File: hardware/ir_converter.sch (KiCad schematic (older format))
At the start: 47 parts, among them J1 MX-47346-0001, J2 SWD, J3 TP, J4 TP, Q1 LL-S350PTC-1A, SW1 RESET, SW2 SW2, U1 TLV70033DDCT, U2 USBLC6-2, U3 STM32F103C8T6

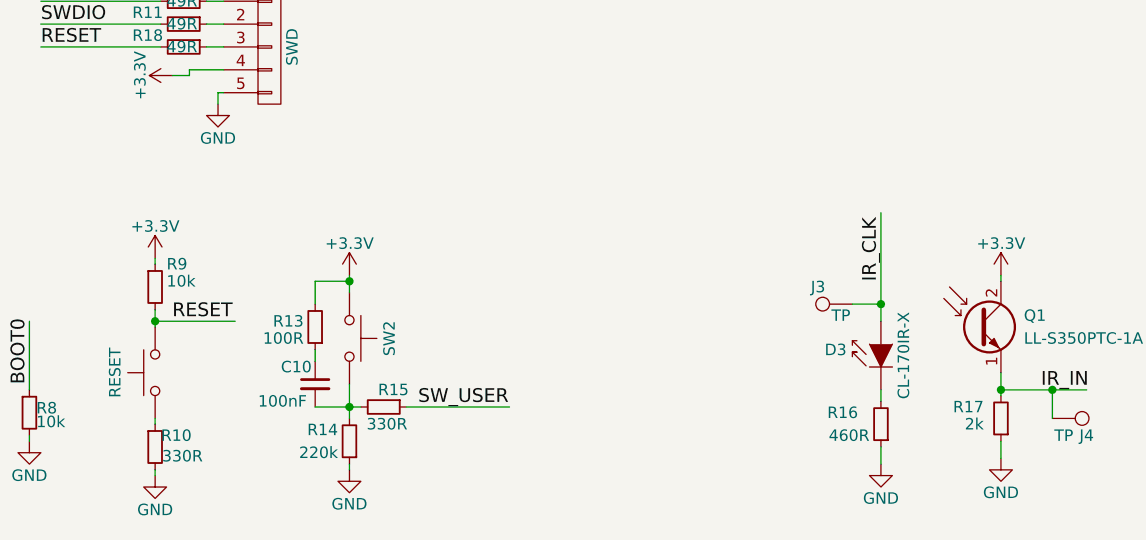
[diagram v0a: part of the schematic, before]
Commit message: Added npn tranistor to drive the IR LED.
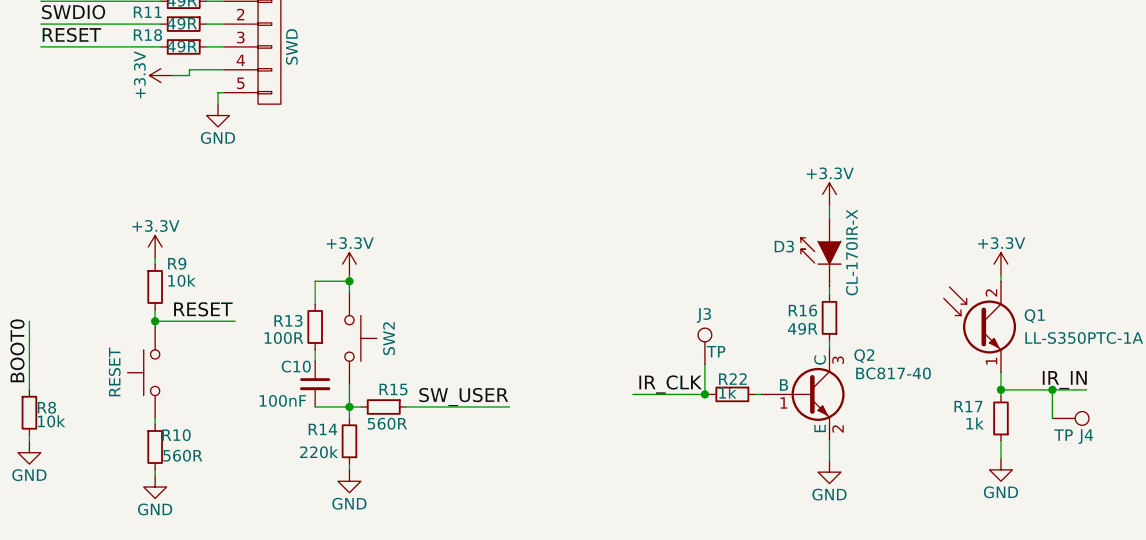
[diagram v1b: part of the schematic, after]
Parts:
- added Q2: BC817-40, TO_SOT_Packages_SMD:SOT-23, symbol BC817-40
- added R22: 1k, Resistors_SMD:R_0603_HandSoldering, symbol R_Small
- R10, R15: value 330R -> 560R
- R16: value 460R -> 49R
- R17: value 2k -> 1k
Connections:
- wire segments 133 -> 136
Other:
- moved on the sheet: D3, J3, R16
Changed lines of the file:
@@
 L IR204A D3
 U 1 1 58E6638F
-P 5725 7000
-F 0 "D3" V 5700 7150 50  0000 L CNN
-F 1 "CL-170IR-X" H 5675 6900 50  0000 C CNN
-F 2 "LEDs:LED_0805" H 5725 7175 50  0001 C CNN
-F 3 "" H 5675 7000 50  0000 C CNN
-	1    5725 7000
+P 5500 6550
+F 0 "D3" V 5475 6700 50  0000 L CNN
+F 1 "CL-170IR-X" H 5450 6450 50  0000 C CNN
+F 2 "LEDs:LED_0805" H 5500 6725 50  0001 C CNN
+F 3 "" H 5450 6550 50  0000 C CNN
+	1    5500 6550
 	0    -1   -1   0
 $EndComp
@@
 L R_Small R16
 U 1 1 58E67683
-P 5725 7350
-F 0 "R16" H 5825 7300 50  0000 L CNN
-F 1 "460R" H 5775 7400 50  0000 L CNN
-F 2 "Resistors_SMD:R_0603_HandSoldering" H 5725 7350 50  0001 C CNN
-F 3 "" H 5725 7350 50  0001 C CNN
-	1    5725 7350
+P 5500 6885
+F 0 "R16" H 5550 6855 50  0000 L CNN
+F 1 "49R" H 5550 6935 50  0000 L CNN
+F 2 "Resistors_SMD:R_0603_HandSoldering" H 5500 6885 50  0001 C CNN
+F 3 "" H 5500 6885 50  0001 C CNN
+	1    5500 6885
 	-1   0    0    1
 $EndComp
@@
 L GND #PWR023
 U 1 1 58E6782D
-P 5725 7525
-F 0 "#PWR023" H 5725 7275 50  0001 C CNN
-F 1 "GND" H 5725 7375 50  0000 C CNN
-F 2 "" H 5725 7525 50  0001 C CNN
-F 3 "" H 5725 7525 50  0001 C CNN
-	1    5725 7525
+P 5500 7510
+F 0 "#PWR023" H 5500 7260 50  0001 C CNN
+F 1 "GND" H 5500 7360 50  0000 C CNN
+F 2 "" H 5500 7510 50  0001 C CNN
+F 3 "" H 5500 7510 50  0001 C CNN
+	1    5500 7510
 	1    0    0    -1
 $EndComp
@@
 P 6250 7325
 F 0 "R17" H 6325 7275 50  0000 L CNN
-F 1 "2k" H 6325 7350 50  0000 L CNN
+F 1 "1k" H 6325 7350 50  0000 L CNN
 F 2 "Resistors_SMD:R_0603_HandSoldering" H 6250 7325 50  0001 C CNN
 F 3 "" H 6250 7325 50  0001 C CNN
@@
 P 2550 7450
 F 0 "R10" H 2575 7500 50  0000 L CNN
-F 1 "330R" H 2580 7410 50  0000 L CNN
+F 1 "560R" H 2580 7410 50  0000 L CNN
 F 2 "Resistors_SMD:R_0603_HandSoldering" H 2550 7450 50  0001 C CNN
 F 3 "" H 2550 7450 50  0001 C CNN
@@
 P 3550 7275
 F 0 "R15" V 3475 7250 50  0000 L CNN
-F 1 "330R" V 3625 7200 50  0000 L CNN
+F 1 "560R" V 3625 7200 50  0000 L CNN
 F 2 "Resistors_SMD:R_0603_HandSoldering" H 3550 7275 50  0001 C CNN
 F 3 "" H 3550 7275 50  0001 C CNN
@@
 Text Label 4100 3300 0    60   ~ 0
 IR_CLK
-Text Label 5725 6725 1    60   ~ 0
+Text Label 4940 7220 2    60   ~ 0
 IR_CLK
 Text Label 6425 7200 0    60   ~ 0
@@
 L TEST_1P J3
 U 1 1 58E9EED0
-P 5600 6825
-F 0 "J3" V 5675 6975 50  0000 C CNN
-F 1 "TP" V 5550 6875 50  0000 C CNN
-F 2 "Measurement_Points:Measurement_Point_Square-SMD-Pad_Big" H 5800 6825 50  0001 C CNN
-F 3 "" H 5800 6825 50  0001 C CNN
-	1    5600 6825
-	0    -1   -1   0
+P 4955 7090
+F 0 "J3" H 4955 7310 50  0000 C CNN
+F 1 "TP" H 5005 7145 50  0000 C CNN
+F 2 "Measurement_Points:Measurement_Point_Square-SMD-Pad_Big" H 5155 7090 50  0001 C CNN
+F 3 "" H 5155 7090 50  0001 C CNN
+	1    4955 7090
+	1    0    0    -1
 $EndComp
 $Comp
@@
 	10400 4300 10875 4300
 Wire Wire Line
-	5725 7450 5725 7525
-Wire Wire Line
-	5725 7250 5725 7200
-Wire Wire Line
-	5725 6425 5725 6900
+	5500 6985 5500 7020
+Wire Wire Line
+	5500 6785 5500 6750
+Wire Wire Line
+	5500 6395 5500 6450
 Wire Wire Line
 	4100 3300 4600 3300
@@
 Wire Wire Line
 	2750 3300 3125 3300
-Wire Wire Line
-	5600 6825 5725 6825
-Connection ~ 5725 6825
 Wire Wire Line
 	6475 7325 6475 7200
@@
 	0    1    1    0
 $EndComp
+$Comp
+L BC817-40 Q2
+U 1 1 590A0634
+P 5400 7220
+F 0 "Q2" H 5605 7390 50  0000 L CNN
+F 1 "BC817-40" H 5610 7310 50  0000 L CNN
+F 2 "TO_SOT_Packages_SMD:SOT-23" H 5600 7145 50  0001 L CIN
+F 3 "" H 5400 7220 50  0001 L CNN
+	1    5400 7220
+	1    0    0    -1
+$EndComp
+Wire Wire Line
+	5500 7420 5500 7510
+$Comp
+L R_Small R22
+U 1 1 590A3C87
+P 5075 7220
+F 0 "R22" V 5010 7155 50  0000 L CNN
+F 1 "1k" V 5070 7155 50  0000 L CNN
+F 2 "Resistors_SMD:R_0603_HandSoldering" H 5075 7220 50  0001 C CNN
+F 3 "" H 5075 7220 50  0001 C CNN
+	1    5075 7220
+	0    1    1    0
+$EndComp
+Wire Wire Line
+	5175 7220 5200 7220
+Wire Wire Line
+	4640 7220 4975 7220
+$Comp
+L +3.3V #PWR035
+U 1 1 590A61E3
+P 5500 6395
+F 0 "#PWR035" H 5500 6245 50  0001 C CNN
+F 1 "+3.3V" H 5500 6535 50  0000 C CNN
+F 2 "" H 5500 6395 50  0001 C CNN
+F 3 "" H 5500 6395 50  0001 C CNN
+	1    5500 6395
+	1    0    0    -1
+$EndComp
+Wire Wire Line
+	4955 7090 4955 7220
+Connection ~ 4955 7220
 $EndSCHEMATC

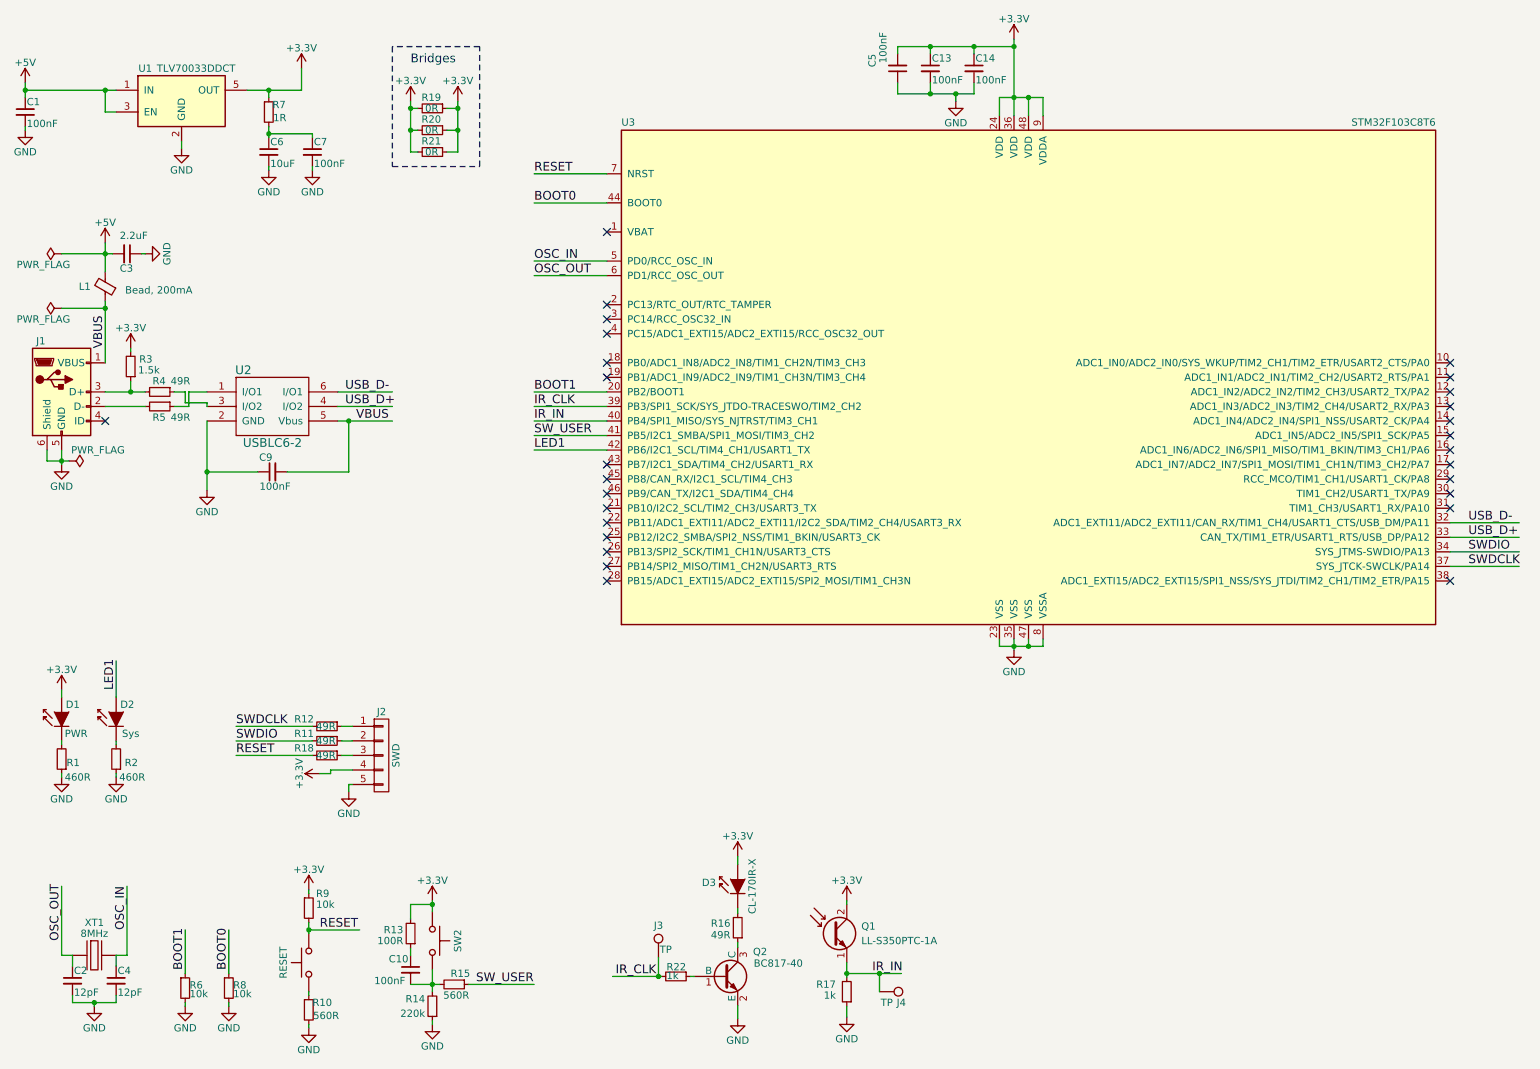
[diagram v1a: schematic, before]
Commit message: Added bug fixes on schematic. Redesigning PCB.
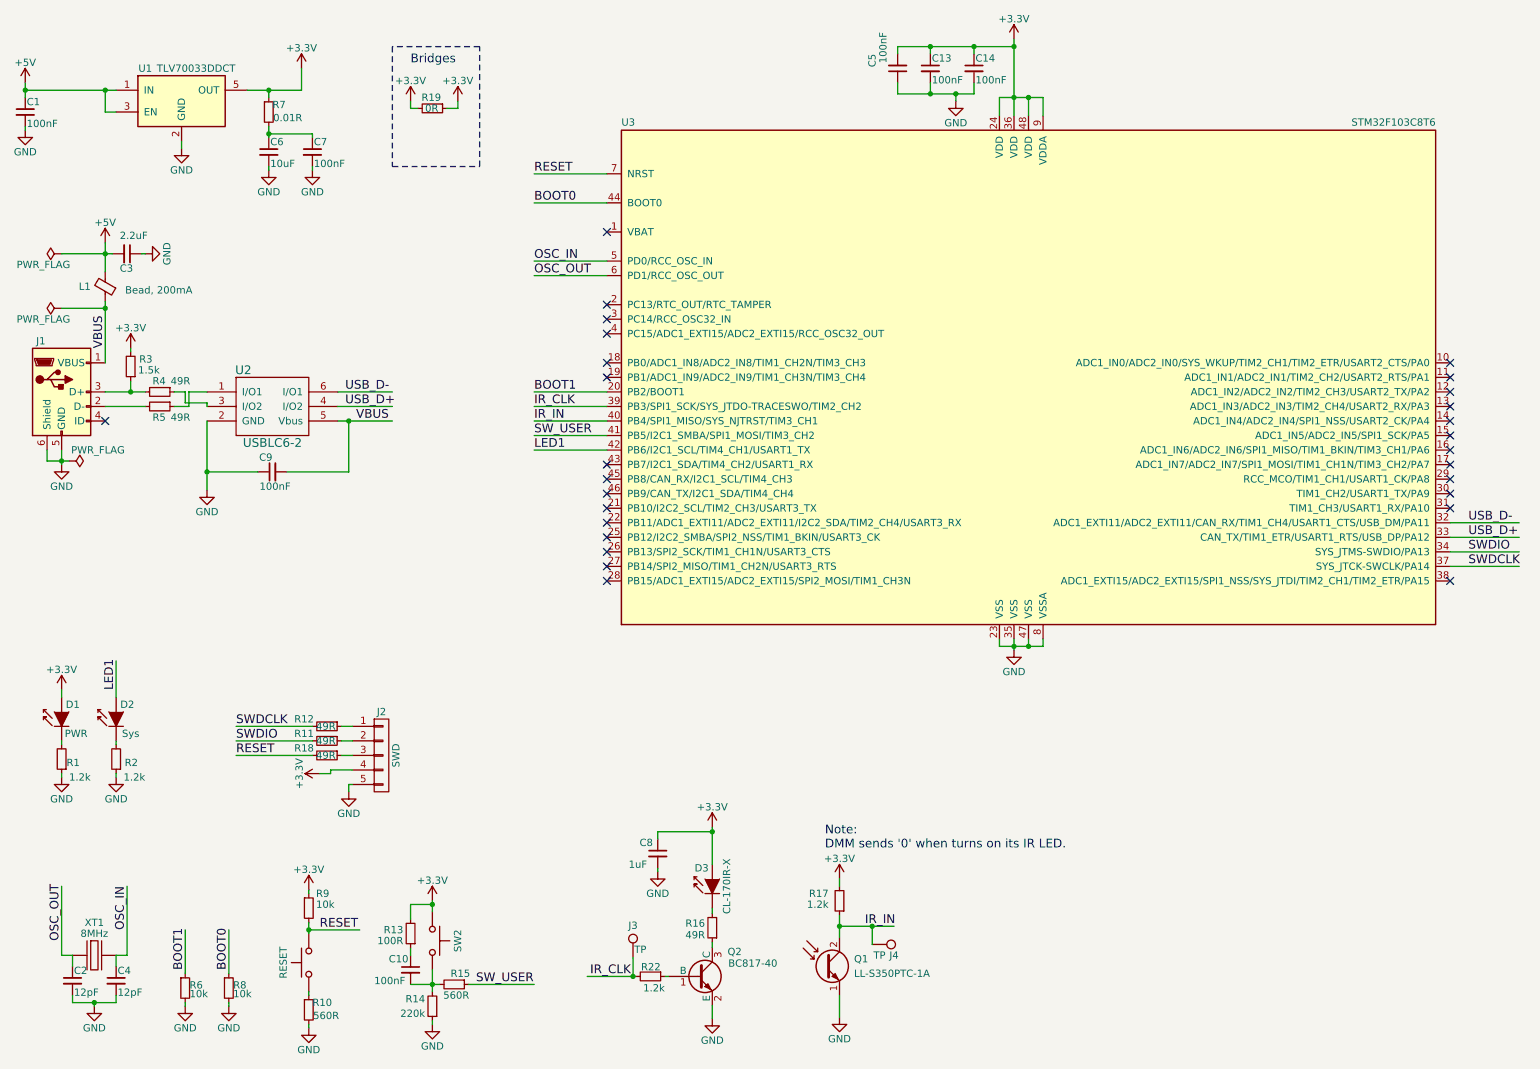
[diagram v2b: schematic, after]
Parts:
- removed R20, R21: 0R, Resistors_SMD:R_1206_HandSoldering, symbol R_Small
- added C8: 1uF, Capacitors_SMD:C_0603_HandSoldering, symbol C_Small
- C14: footprint Capacitors_SMD:C_1206_HandSoldering -> Capacitors_SMD:C_0603_HandSoldering
- C6: footprint Capacitors_SMD:C_1206 -> Capacitors_SMD:C_0603_HandSoldering
- D1, D2: footprint LEDs:LED_0805 -> LEDs:LED_1206
- J3, J4: footprint Measurement_Points:Measurement_Point_Square-SMD-Pad_Big -> Measurement_Points:Measurement_Point_Square-SMD-Pad_Small
- R1, R2: value 460R -> 1.2k
- R17, R22: value 1k -> 1.2k
- R6: footprint Resistors_SMD:R_0805 -> Resistors_SMD:R_0603_HandSoldering
- R7: value 1R -> 0.01R
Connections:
- wire segments 136 -> 135
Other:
- note added: "Note:\nDMM sends '0' when turns on its IR LED."
- moved on the sheet: D3, J3, J4, Q1, Q2, R16, R17, R22

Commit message: Elements arrangement.
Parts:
- removed R19: 0R, Resistors_SMD:R_1206_HandSoldering, symbol R_Small
- removed R7: 0.01R, Resistors_SMD:R_0603_HandSoldering, symbol R_Small
- R18: footprint Resistors_SMD:R_0805 -> Resistors_SMD:R_0603_HandSoldering
- R3: footprint Resistors_SMD:R_1206_HandSoldering -> Resistors_SMD:R_0603_HandSoldering
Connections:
- net labels added: S_D+, S_D-
- wire segments 135 -> 129
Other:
- note removed: "Bridges"
- moved on the sheet: C6, C7
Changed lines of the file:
@@
 L GND #PWR02
 U 1 1 58E4A167
-P 2275 1675
-F 0 "#PWR02" H 2275 1425 50  0001 C CNN
-F 1 "GND" H 2275 1525 50  0000 C CNN
-F 2 "" H 2275 1675 50  0001 C CNN
-F 3 "" H 2275 1675 50  0001 C CNN
-	1    2275 1675
-	1    0    0    -1
-$EndComp
-$Comp
-L R_Small R7
-U 1 1 58E4A190
-P 2275 1275
-F 0 "R7" H 2300 1325 50  0000 L CNN
-F 1 "0.01R" H 2305 1235 50  0000 L CNN
-F 2 "Resistors_SMD:R_0603_HandSoldering" H 2275 1275 50  0001 C CNN
-F 3 "" H 2275 1275 50  0001 C CNN
-	1    2275 1275
+P 2200 1450
+F 0 "#PWR02" H 2200 1200 50  0001 C CNN
+F 1 "GND" H 2200 1300 50  0000 C CNN
+F 2 "" H 2200 1450 50  0001 C CNN
+F 3 "" H 2200 1450 50  0001 C CNN
+	1    2200 1450
 	1    0    0    -1
 $EndComp
@@
 L C_Small C6
 U 1 1 58E4A225
-P 2275 1550
-F 0 "C6" H 2285 1620 50  0000 L CNN
-F 1 "10uF" H 2285 1470 50  0000 L CNN
-F 2 "Capacitors_SMD:C_0603_HandSoldering" H 2275 1550 50  0001 C CNN
-F 3 "" H 2275 1550 50  0001 C CNN
-	1    2275 1550
+P 2200 1325
+F 0 "C6" H 2210 1395 50  0000 L CNN
+F 1 "10uF" H 2210 1245 50  0000 L CNN
+F 2 "Capacitors_SMD:C_0603_HandSoldering" H 2200 1325 50  0001 C CNN
+F 3 "" H 2200 1325 50  0001 C CNN
+	1    2200 1325
 	1    0    0    -1
 $EndComp
@@
 L C_Small C7
 U 1 1 58E4A432
-P 2575 1550
-F 0 "C7" H 2585 1620 50  0000 L CNN
-F 1 "100nF" H 2585 1470 50  0000 L CNN
-F 2 "Capacitors_SMD:C_0603_HandSoldering" H 2575 1550 50  0001 C CNN
-F 3 "" H 2575 1550 50  0001 C CNN
-	1    2575 1550
+P 2425 1325
+F 0 "C7" H 2435 1395 50  0000 L CNN
+F 1 "100nF" H 2435 1245 50  0000 L CNN
+F 2 "Capacitors_SMD:C_0603_HandSoldering" H 2425 1325 50  0001 C CNN
+F 3 "" H 2425 1325 50  0001 C CNN
+	1    2425 1325
 	1    0    0    -1
 $EndComp
@@
 L GND #PWR04
 U 1 1 58E4A63E
-P 2575 1675
-F 0 "#PWR04" H 2575 1425 50  0001 C CNN
-F 1 "GND" H 2575 1525 50  0000 C CNN
-F 2 "" H 2575 1675 50  0001 C CNN
-F 3 "" H 2575 1675 50  0001 C CNN
-	1    2575 1675
+P 2425 1450
+F 0 "#PWR04" H 2425 1200 50  0001 C CNN
+F 1 "GND" H 2425 1300 50  0000 C CNN
+F 2 "" H 2425 1450 50  0001 C CNN
+F 3 "" H 2425 1450 50  0001 C CNN
+	1    2425 1450
 	1    0    0    -1
 $EndComp
@@
 F 0 "R3" H 1175 2975 50  0000 L CNN
 F 1 "1.5k" H 1125 3050 50  0000 L CNN
-F 2 "Resistors_SMD:R_1206_HandSoldering" H 1325 3025 50  0001 C CNN
+F 2 "Resistors_SMD:R_0603_HandSoldering" H 1325 3025 50  0001 C CNN
 F 3 "" H 1325 3025 50  0001 C CNN
 	1    1325 3025
@@
 F 0 "R18" V 2625 5475 50  0000 L CNN
 F 1 "49R" V 2675 5625 50  0000 L CNN
-F 2 "Resistors_SMD:R_0805" H 2675 5700 50  0001 C CNN
+F 2 "Resistors_SMD:R_0603_HandSoldering" H 2675 5700 50  0001 C CNN
 F 3 "" H 2675 5700 50  0001 C CNN
 	1    2675 5700
@@
 NoConn ~ 4600 4200
 $Comp
-L R_Small R19
-U 1 1 58E7CB35
-P 3400 1250
-F 0 "R19" V 3325 1175 50  0000 L CNN
-F 1 "0R" V 3400 1200 50  0000 L CNN
-F 2 "Resistors_SMD:R_1206_HandSoldering" H 3400 1250 50  0001 C CNN
-F 3 "" H 3400 1250 50  0001 C CNN
-	1    3400 1250
-	0    1    1    0
-$EndComp
-$Comp
-L +3.3V #PWR032
-U 1 1 58E7CECF
-P 3250 1200
-F 0 "#PWR032" H 3250 1050 50  0001 C CNN
-F 1 "+3.3V" H 3250 1340 50  0000 C CNN
-F 2 "" H 3250 1200 50  0001 C CNN
-F 3 "" H 3250 1200 50  0001 C CNN
-	1    3250 1200
-	1    0    0    -1
-$EndComp
-$Comp
-L +3.3V #PWR033
-U 1 1 58E7CF5E
-P 3575 1200
-F 0 "#PWR033" H 3575 1050 50  0001 C CNN
-F 1 "+3.3V" H 3575 1340 50  0000 C CNN
-F 2 "" H 3575 1200 50  0001 C CNN
-F 3 "" H 3575 1200 50  0001 C CNN
-	1    3575 1200
-	1    0    0    -1
-$EndComp
-$Comp
-L PWR_FLAG #FLG034
+L PWR_FLAG #FLG032
 U 1 1 58E7DF60
 P 850 2625
-F 0 "#FLG034" H 850 2700 50  0001 C CNN
+F 0 "#FLG032" H 850 2700 50  0001 C CNN
 F 1 "PWR_FLAG" V 775 2750 50  0000 C CNN
 F 2 "" H 850 2625 50  0001 C CNN
@@
 	2125 1125 2500 1125
 Wire Wire Line
-	2275 1375 2275 1450
-Wire Wire Line
-	2275 1650 2275 1675
+	2200 1425 2200 1450
 Wire Wire Line
 	600  1125 1225 1125
@@
 Wire Wire Line
 	600  1075 600  1175
-Connection ~ 2275 1125
-Wire Wire Line
-	2575 1650 2575 1675
+Wire Wire Line
+	2425 1425 2425 1450
 Connection ~ 600  1125
 Wire Wire Line
@@
 	4100 2400 4600 2400
 Wire Wire Line
-	2275 1125 2275 1175
-Wire Wire Line
 	7600 1175 7600 1300
 Connection ~ 7500 1175
@@
 	1850 3275 1850 3300
 Wire Wire Line
-	2575 1450 2575 1425
-Wire Wire Line
-	2575 1425 2275 1425
-Connection ~ 2275 1425
-Wire Wire Line
 	2850 5900 2825 5900
 Wire Wire Line
@@
 	6600 1075 6600 1150
 Connection ~ 6825 1150
-Wire Wire Line
-	3500 1250 3575 1250
-Wire Wire Line
-	3300 1250 3250 1250
-Text Notes 3250 950  0    60   ~ 0
-Bridges
-Wire Notes Line
-	3125 825  3125 1650
-Wire Notes Line
-	3125 1650 3725 1650
-Wire Notes Line
-	3725 1650 3725 825
-Wire Notes Line
-	3725 825  3125 825
 $Comp
 L SW_Push SW2
@@
 	4465 7220 4800 7220
 $Comp
-L +3.3V #PWR035
+L +3.3V #PWR033
 U 1 1 590A61E3
 P 5325 6195
-F 0 "#PWR035" H 5325 6045 50  0001 C CNN
+F 0 "#PWR033" H 5325 6045 50  0001 C CNN
 F 1 "+3.3V" H 5325 6335 50  0000 C CNN
 F 2 "" H 5325 6195 50  0001 C CNN
@@
 	4950 6500 4950 6475
 $Comp
-L GND #PWR036
+L GND #PWR034
 U 1 1 5924FDA3
 P 4950 6500
-F 0 "#PWR036" H 4950 6250 50  0001 C CNN
+F 0 "#PWR034" H 4950 6250 50  0001 C CNN
 F 1 "GND" H 4950 6350 50  0000 C CNN
 F 2 "" H 4950 6500 50  0001 C CNN
@@
 $EndComp
 Wire Wire Line
-	3575 1250 3575 1200
-Wire Wire Line
-	3250 1250 3250 1200
+	2425 1225 2425 1125
+Connection ~ 2425 1125
+Wire Wire Line
+	2200 1225 2200 1125
+Connection ~ 2200 1125
+Text Label 1150 3200 0    60   ~ 0
+S_D+
+Text Label 1150 3300 0    60   ~ 0
+S_D-
 $EndSCHEMATC

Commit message: Almost done.
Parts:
- D3: footprint LEDs:LED_0805 -> CustomFootprints:IR_LED_WIDE
- Q1: footprint LEDs:LED_1206 -> CustomFootprints:IR_PHOTO_WIDE
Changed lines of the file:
@@
 F 0 "D3" V 5400 6575 50  0000 L CNN
 F 1 "CL-170IR-X" H 5275 6450 50  0000 C CNN
-F 2 "LEDs:LED_0805" H 5325 6725 50  0001 C CNN
+F 2 "CustomFootprints:IR_LED_WIDE" H 5325 6725 50  0001 C CNN
 F 3 "" H 5275 6550 50  0000 C CNN
 	1    5325 6550
@@
 F 0 "Q1" H 6300 7200 50  0000 L CNN
 F 1 "LL-S350PTC-1A" H 6300 7100 50  0000 L CNN
-F 2 "LEDs:LED_1206" H 6300 7250 50  0001 C CNN
+F 2 "CustomFootprints:IR_PHOTO_WIDE" H 6300 7250 50  0001 C CNN
 F 3 "" H 6100 7150 50  0001 C CNN
 	1    6100 7150
